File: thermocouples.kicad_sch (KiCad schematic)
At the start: 52 parts, among them J300 Conn_01x02_Pin, J301 Conn_01x02_Pin, J302 Conn_01x02_Pin, J303 Conn_01x02_Pin, U300 MAX31856, U301 MAX31856, U302 MAX31856, U303 MAX31856

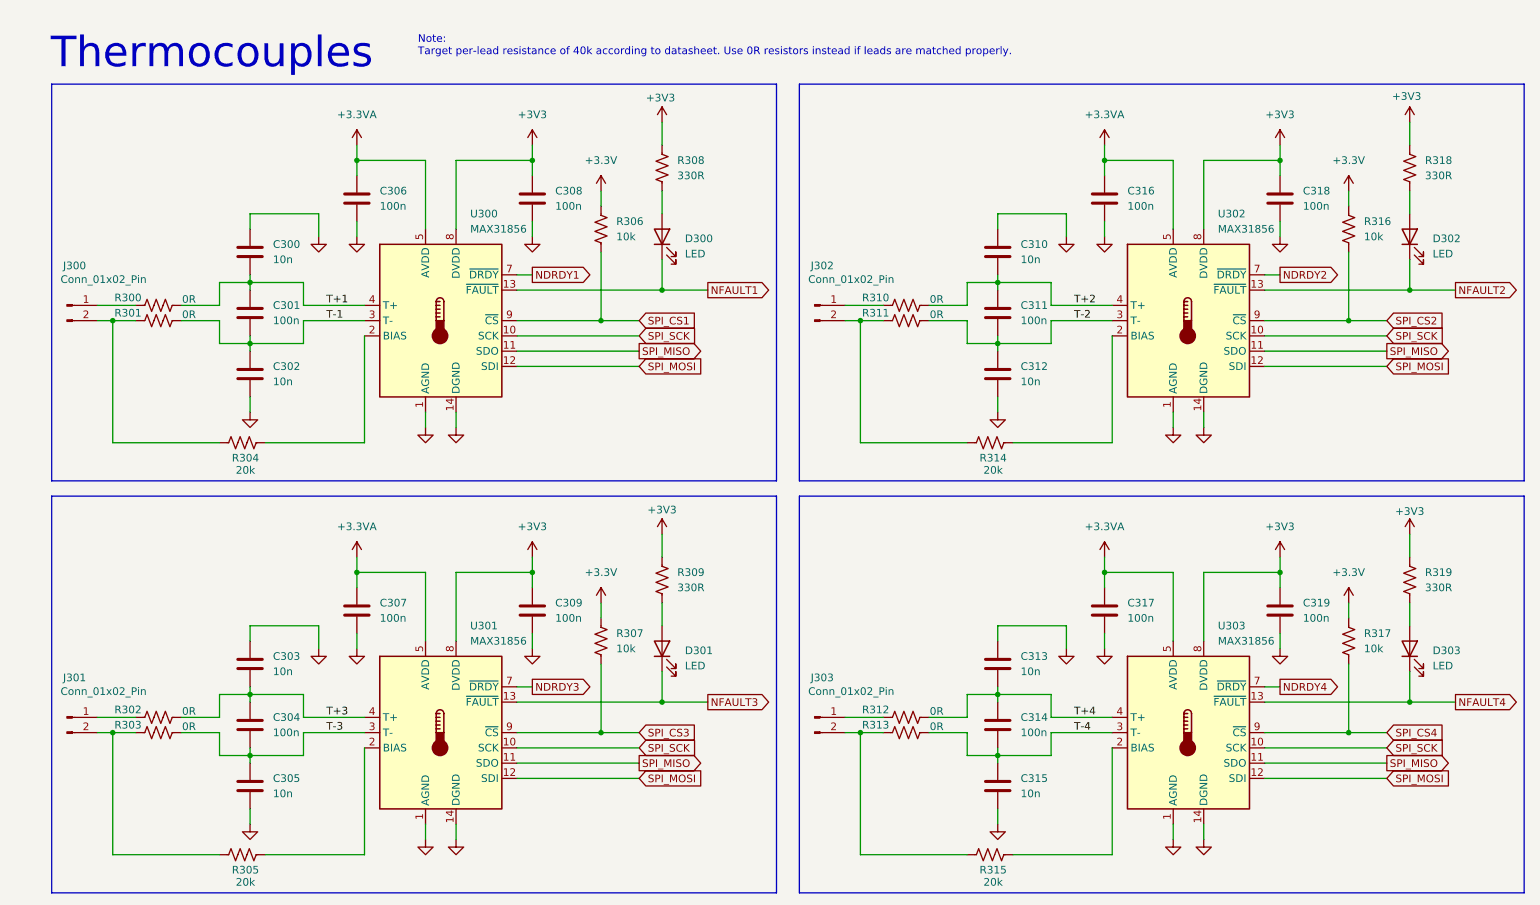
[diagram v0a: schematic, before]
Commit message: Footprints added
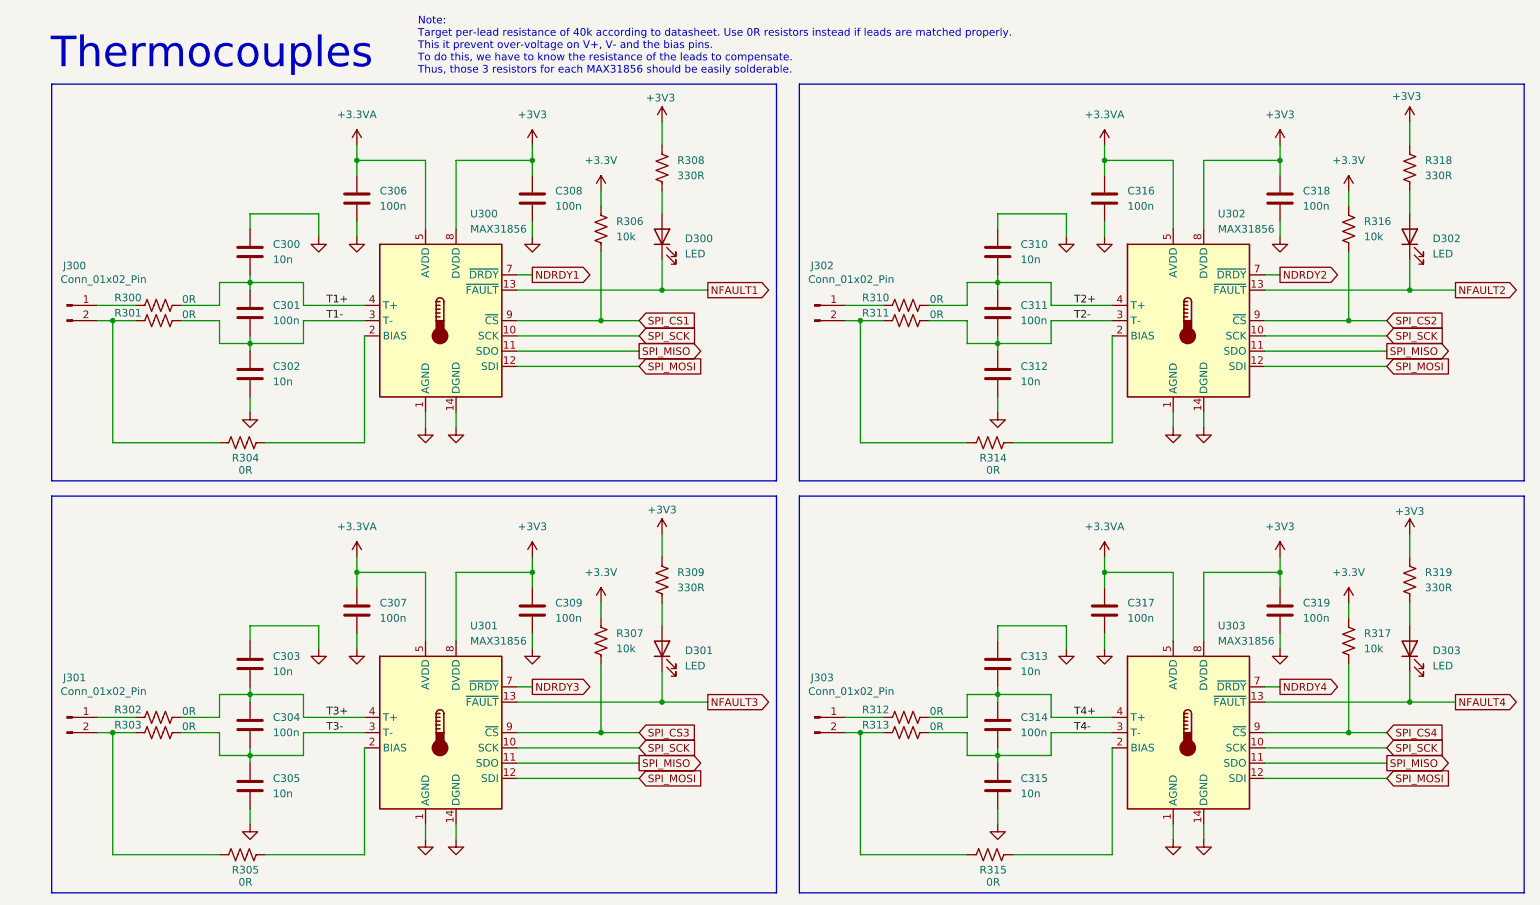
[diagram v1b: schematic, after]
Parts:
- C300, C301, C302, C303, C304, C305, C306, C307, C308, C309, C310, C311, C312, C313, C314, C315, C316, C317, C318, C319, D300, D301, D302, D303: footprint (none) -> Capacitor_SMD:C_01005_0402Metric
- J300, J301, J302, J303: footprint (none) -> Connector_PinHeader_2.54mm:PinHeader_1x02_P2.54mm_Vertical
- R300, R301, R302, R303, R310, R311, R312, R313: footprint (none) -> Resistor_SMD:R_0201_0603Metric
- R304, R305, R314, R315: value 20k -> 0R; footprint (none) -> Resistor_SMD:R_0201_0603Metric
- R306, R307, R308, R309, R316, R317, R318, R319: footprint (none) -> Resistor_SMD:R_01005_0402Metric
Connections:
- net T+1 renamed T1+
- net T+2 renamed T2+
- net T+3 renamed T3+
- net T+4 renamed T4+
- net T-1 renamed T1-
- net T-2 renamed T2-
- net T-3 renamed T3-
- net T-4 renamed T4-
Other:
- note added: "Note: Target per-lead resistance of 40k according to datasheet. Use 0R resistors instead if leads are matched properly. This it prevent over-voltage on V+, V- and the bias pins. To do this, we have to know the resistance of the leads to compensate. Thus, those 3 resistors for each MAX31856 should be easily solderable."
- note removed: "Note: Target per-lead resistance of 40k according to datasheet. Use 0R resistors instead if leads are matched properly."
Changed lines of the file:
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@@
 		)
 	)
-	(text "Note:\nTarget per-lead resistance of 40k according to datasheet. Use 0R resistors instead if leads are matched properly."
+	(text "Note:\nTarget per-lead resistance of 40k according to datasheet. Use 0R resistors instead if leads are matched properly.\nThis it prevent over-voltage on V+, V- and the bias pins.\nTo do this, we have to know the resistance of the leads to compensate.\nThus, those 3 resistors for each MAX31856 should be easily solderable."
 		(exclude_from_sim no)
 		(at 78.74 19.05 0)
@@
 		)
 	)
-	(label "T-4"
+	(label "T4-"
 		(at 187.96 133.35 0)
 		(effects
@@
 		)
 	)
-	(label "T-2"
+	(label "T2-"
 		(at 187.96 64.77 0)
 		(effects
@@
 		)
 	)
-	(label "T+2"
+	(label "T2+"
 		(at 187.96 62.23 0)
 		(effects
@@
 		)
 	)
-	(label "T+1"
+	(label "T1+"
 		(at 63.5 62.23 0)
 		(effects
@@
 		)
 	)
-	(label "T+3"
+	(label "T3+"
 		(at 63.5 130.81 0)
 		(effects
@@
 		)
 	)
-	(label "T+4"
+	(label "T4+"
 		(at 187.96 130.81 0)
 		(effects
@@
 		)
 	)
-	(label "T-3"
+	(label "T3-"
 		(at 63.5 133.35 0)
 		(effects
@@
 		)
 	)
-	(label "T-1"
+	(label "T1-"
 		(at 63.5 64.77 0)
 		(effects
@@
 			)
 		)
-		(property "Value" "20k"
+		(property "Value" "0R"
 			(at 174.498 89.662 90)
 			(effects
@@
 			)
 		)
-		(property "Footprint" ""
+		(property "Footprint" "Resistor_SMD:R_0201_0603Metric"
 			(at 174.244 84.074 90)
 			(effects
@@
 			)
 		)
-		(property "Footprint" ""
+		(property "Footprint" "Resistor_SMD:R_01005_0402Metric"
 			(at 244.856 108.204 90)
 			(effects
@@
 			)
 		)
-		(property "Footprint" ""
+		(property "Footprint" "Capacitor_SMD:C_01005_0402Metric"
 			(at 69.5452 116.84 0)
 			(effects
@@
 			)
 		)
-		(property "Footprint" ""
+		(property "Footprint" "Resistor_SMD:R_0201_0603Metric"
 			(at 35.814 61.214 90)
 			(effects
@@
 			)
 		)
-		(property "Footprint" ""
+		(property "Footprint" "Capacitor_SMD:C_01005_0402Metric"
 			(at 194.0052 48.26 0)
 			(effects
@@
 			)
 		)
-		(property "Footprint" ""
+		(property "Footprint" "Capacitor_SMD:C_01005_0402Metric"
 			(at 98.7552 48.26 0)
 			(effects
@@
 			)
 		)
-		(property "Footprint" ""
+		(property "Footprint" "Resistor_SMD:R_0201_0603Metric"
 			(at 160.274 63.754 90)
 			(effects
@@
 			)
 		)
-		(property "Footprint" ""
+		(property "Footprint" "Capacitor_SMD:C_01005_0402Metric"
 			(at 51.7652 125.73 0)
 			(effects
@@
 			)
 		)
-		(property "Footprint" ""
+		(property "Footprint" "Resistor_SMD:R_0201_0603Metric"
 			(at 160.274 61.214 90)
 			(effects
@@
 			)
 		)
-		(property "Footprint" ""
+		(property "Footprint" "Resistor_SMD:R_0201_0603Metric"
 			(at 35.814 129.794 90)
 			(effects
@@
 			)
 		)
-		(property "Footprint" ""
+		(property "Footprint" "Resistor_SMD:R_01005_0402Metric"
 			(at 120.396 39.624 90)
 			(effects
@@
 			)
 		)
-		(property "Footprint" ""
+		(property "Footprint" "Capacitor_SMD:C_01005_0402Metric"
 			(at 51.7652 135.89 0)
 			(effects
@@
 			)
 		)
-		(property "Footprint" ""
+		(property "Footprint" "Connector_PinHeader_2.54mm:PinHeader_1x02_P2.54mm_Vertical"
 			(at 144.78 62.23 0)
 			(effects
@@
 			)
 		)
-		(property "Footprint" ""
+		(property "Footprint" "Connector_PinHeader_2.54mm:PinHeader_1x02_P2.54mm_Vertical"
 			(at 20.32 130.81 0)
 			(effects
@@
 			)
 		)
-		(property "Footprint" ""
+		(property "Footprint" "Resistor_SMD:R_0201_0603Metric"
 			(at 35.814 132.334 90)
 			(effects
@@
 			)
 		)
-		(property "Footprint" ""
+		(property "Footprint" "Resistor_SMD:R_0201_0603Metric"
 			(at 160.274 132.334 90)
 			(effects
@@
 			)
 		)
-		(property "Footprint" ""
+		(property "Footprint" "Capacitor_SMD:C_01005_0402Metric"
 			(at 51.7652 57.15 0)
 			(effects
@@
 			)
 		)
-		(property "Footprint" ""
+		(property "Footprint" "Capacitor_SMD:C_01005_0402Metric"
 			(at 98.7552 116.84 0)
 			(effects
@@
 			)
 		)
-		(property "Footprint" ""
+		(property "Footprint" "Capacitor_SMD:C_01005_0402Metric"
 			(at 176.2252 135.89 0)
 			(effects
@@
 			)
 		)
-		(property "Footprint" ""
+		(property "Footprint" "Capacitor_SMD:C_01005_0402Metric"
 			(at 176.2252 125.73 0)
 			(effects
@@
 			)
 		)
-		(property "Footprint" ""
+		(property "Footprint" "Resistor_SMD:R_01005_0402Metric"
 			(at 120.396 108.204 90)
 			(effects
@@
 			)
 		)
-		(property "Footprint" ""
+		(property "Footprint" "Capacitor_SMD:C_01005_0402Metric"
 			(at 176.2252 57.15 0)
 			(effects
@@
 			)
 		)
-		(property "Footprint" ""
+		(property "Footprint" "Capacitor_SMD:C_01005_0402Metric"
 			(at 51.7652 77.47 0)
 			(effects
@@
 			)
 		)
-		(property "Footprint" ""
+		(property "Footprint" "Connector_PinHeader_2.54mm:PinHeader_1x02_P2.54mm_Vertical"
 			(at 20.32 62.23 0)
 			(effects
@@
 			)
 		)
-		(property "Footprint" ""
+		(property "Footprint" "Capacitor_SMD:C_01005_0402Metric"
 			(at 176.2252 146.05 0)
 			(effects
@@
 			)
 		)
-		(property "Footprint" ""
+		(property "Footprint" "Resistor_SMD:R_01005_0402Metric"
 			(at 234.696 49.784 90)
 			(effects
@@
 			)
 		)
-		(property "Footprint" ""
+		(property "Footprint" "Resistor_SMD:R_0201_0603Metric"
 			(at 160.274 129.794 90)
 			(effects
@@
 			)
 		)
-		(property "Value" "20k"
+		(property "Value" "0R"
 			(at 50.038 158.242 90)
 			(effects
@@
 			)
 		)
-		(property "Footprint" ""
+		(property "Footprint" "Resistor_SMD:R_0201_0603Metric"
 			(at 49.784 152.654 90)
 			(effects
@@
 			)
 		)
-		(property "Footprint" ""
+		(property "Footprint" "Capacitor_SMD:C_01005_0402Metric"
 			(at 243.84 50.8 0)
 			(effects
@@
 			)
 		)
-		(property "Footprint" ""
+		(property "Footprint" "Resistor_SMD:R_01005_0402Metric"
 			(at 234.696 118.364 90)
 			(effects
@@
 			)
 		)
-		(property "Footprint" ""
+		(property "Footprint" "Capacitor_SMD:C_01005_0402Metric"
 			(at 69.5452 48.26 0)
 			(effects
@@
 			)
 		)
-		(property "Footprint" ""
+		(property "Footprint" "Capacitor_SMD:C_01005_0402Metric"
 			(at 176.2252 77.47 0)
 			(effects
@@
 			)
 		)
-		(property "Footprint" ""
+		(property "Footprint" "Resistor_SMD:R_01005_0402Metric"
 			(at 110.236 49.784 90)
 			(effects
@@
 			)
 		)
-		(property "Footprint" ""
+		(property "Footprint" "Resistor_SMD:R_0201_0603Metric"
 			(at 35.814 63.754 90)
 			(effects
@@
 			)
 		)
-		(property "Footprint" ""
+		(property "Footprint" "Capacitor_SMD:C_01005_0402Metric"
 			(at 51.7652 67.31 0)
 			(effects
@@
 			)
 		)
-		(property "Footprint" ""
+		(property "Footprint" "Resistor_SMD:R_01005_0402Metric"
 			(at 244.856 39.624 90)
 			(effects
@@
 			)
 		)
-		(property "Footprint" ""
+		(property "Footprint" "Capacitor_SMD:C_01005_0402Metric"
 			(at 194.0052 116.84 0)
 			(effects
@@
 			)
 		)
-		(property "Footprint" ""
+		(property "Footprint" "Resistor_SMD:R_01005_0402Metric"
 			(at 110.236 118.364 90)
 			(effects
@@
 			)
 		)
-		(property "Footprint" ""
+		(property "Footprint" "Capacitor_SMD:C_01005_0402Metric"
 			(at 119.38 50.8 0)
 			(effects
@@
 			)
 		)
-		(property "Footprint" ""
+		(property "Footprint" "Capacitor_SMD:C_01005_0402Metric"
 			(at 223.2152 48.26 0)
 			(effects
@@
 			)
 		)
-		(property "Footprint" ""
+		(property "Footprint" "Capacitor_SMD:C_01005_0402Metric"
 			(at 51.7652 146.05 0)
 			(effects
@@
 			)
 		)
-		(property "Footprint" ""
+		(property "Footprint" "Connector_PinHeader_2.54mm:PinHeader_1x02_P2.54mm_Vertical"
 			(at 144.78 130.81 0)
 			(effects
@@
 			)
 		)
-		(property "Footprint" ""
+		(property "Footprint" "Capacitor_SMD:C_01005_0402Metric"
 			(at 176.2252 67.31 0)
 			(effects
@@
 			)
 		)
-		(property "Footprint" ""
+		(property "Footprint" "Capacitor_SMD:C_01005_0402Metric"
 			(at 223.2152 116.84 0)
 			(effects
@@
 			)
 		)
-		(property "Value" "20k"
+		(property "Value" "0R"
 			(at 50.038 89.662 90)
 			(effects
@@
 			)
 		)
-		(property "Footprint" ""
+		(property "Footprint" "Resistor_SMD:R_0201_0603Metric"
 			(at 49.784 84.074 90)
 			(effects
@@
 			)
 		)
-		(property "Value" "20k"
+		(property "Value" "0R"
 			(at 174.498 158.242 90)
 			(effects
@@
 			)
 		)
-		(property "Footprint" ""
+		(property "Footprint" "Resistor_SMD:R_0201_0603Metric"
 			(at 174.244 152.654 90)
 			(effects
@@
 			)
 		)
-		(property "Footprint" ""
+		(property "Footprint" "Capacitor_SMD:C_01005_0402Metric"
 			(at 243.84 119.38 0)
 			(effects
@@
 			)
 		)
-		(property "Footprint" ""
+		(property "Footprint" "Capacitor_SMD:C_01005_0402Metric"
 			(at 119.38 119.38 0)
 			(effects
